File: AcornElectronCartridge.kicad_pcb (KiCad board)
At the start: 2 copper layers, 84.9 x 62.5 mm, 5 parts

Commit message: An intermediate version of a smaller cartridge.
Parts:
- moved Flash1 8.89 mm to (86.4, 104.1)
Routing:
- net /A16: track 82.4 -> 93.0 mm
- net /A10: track 83.4 -> 93.4 mm
- net /A15: track 85.7 -> 95.6 mm
- net /A8: track 56.5 -> 46.8 mm
- net /CSRW: track 84.2 -> 93.6 mm
- net /CE#: track 22.9 -> 31.8 mm
- net /BA7: track 27.2 -> 18.4 mm
- net /BA6: track 27.2 -> 18.4 mm
- net /BA4: track 27.2 -> 18.4 mm
- net /BA3: track 27.2 -> 18.4 mm
- net /BA2: track 27.2 -> 18.4 mm
- net /BA5: track 27.2 -> 18.4 mm
- net /A14: track 5.68 -> 14.2 mm
- net /OE#: track 5.68 -> 14.2 mm
- net /D2: track 26.2 -> 17.8 mm
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
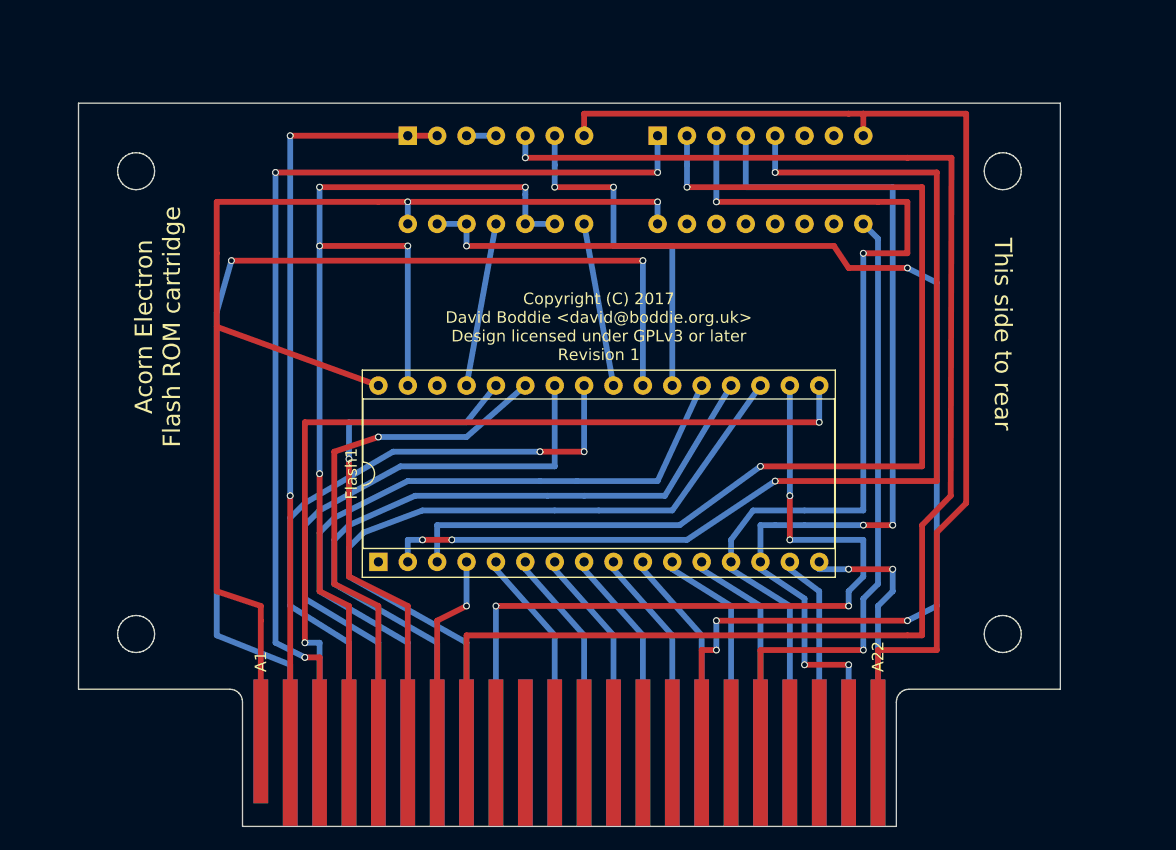
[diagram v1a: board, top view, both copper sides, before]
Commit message: Made space at the top of the board.
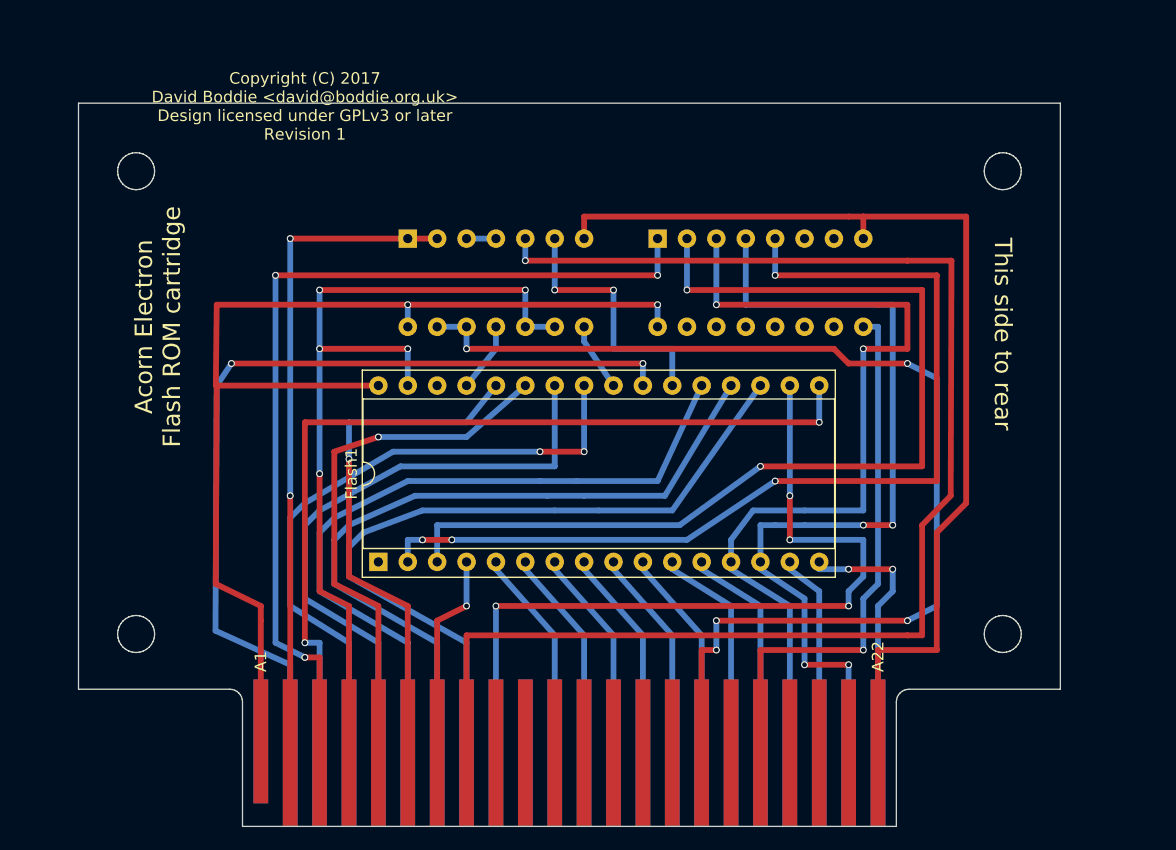
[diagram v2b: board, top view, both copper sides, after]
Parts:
- moved FLIP1 8.89 mm to (110.5, 76.2)
- moved NAND1 8.89 mm to (88.9, 76.2)
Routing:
- net /CSRW: track 93.6 -> 75.9 mm
- net /A10: track 93.4 -> 75.7 mm
- net VCC: track 106.1 -> 96.0 mm
- net GND: track 121.6 -> 112.7 mm
- net /nRST: track 89.2 -> 80.3 mm
- net /nOE: track 66.0 -> 57.2 mm
- net /D1: track 83.3 -> 74.4 mm
- net /CE#: track 31.8 -> 22.9 mm
- net /A15: track 95.6 -> 86.7 mm
- net /D0: track 86.6 -> 77.7 mm
- net /A16: track 93.0 -> 84.1 mm
- net /PHI2: track 130.5 -> 121.7 mm
- net /ROMQA: track 106.4 -> 97.6 mm
- net /OE#: track 14.2 -> 5.85 mm
- net /A14: track 14.2 -> 5.97 mm
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
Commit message: Finished a first draft of the smaller cartridge design.
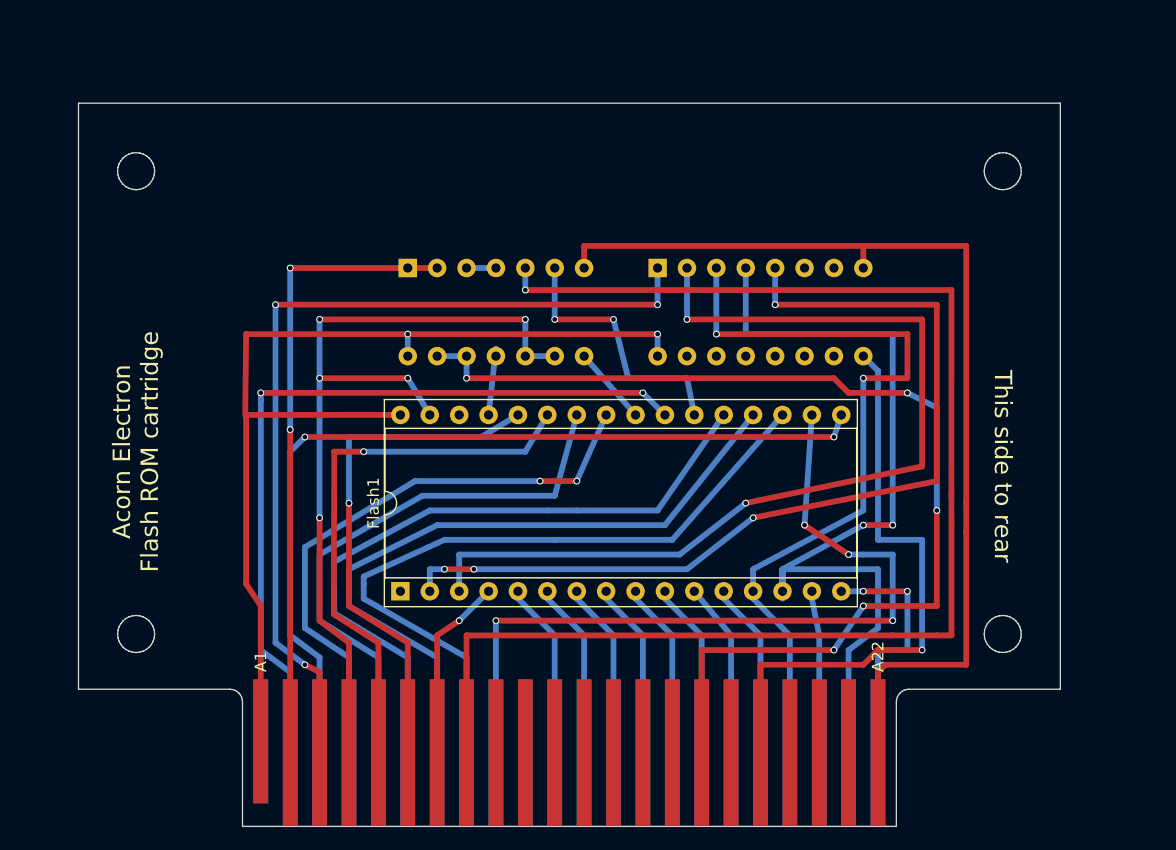
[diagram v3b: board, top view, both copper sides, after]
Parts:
- moved Flash1 3.18 mm to (88.3, 106.7)
- moved FLIP1 2.54 mm to (110.5, 78.7)
- moved NAND1 2.54 mm to (88.9, 78.7)
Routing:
- net /D0: track 77.7 -> 69.3 mm
- net VCC: track 96.0 -> 88.3 mm
- net /A10: track 75.7 -> 68.1 mm
- net /A11: track 56.0 -> 51.2 mm
- net /A9: track 53.4 -> 48.9 mm
- net /nROMSTB: track 47.5 -> 51.9 mm
- net /A15: track 86.7 -> 82.5 mm
- net /A16: track 84.1 -> 79.9 mm
- net /BA0: track 19.3 -> 15.3 mm
- net /D7: track 63.0 -> 59.2 mm
- net /D2: track 17.8 -> 14.0 mm
- net /D6: track 64.3 -> 60.7 mm
- net /D5: track 65.7 -> 62.2 mm
- net /BA1: track 19.3 -> 15.8 mm
- net /ROMQA: track 97.6 -> 94.3 mm
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
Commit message: Placed the smaller chips beside the flash ROM.
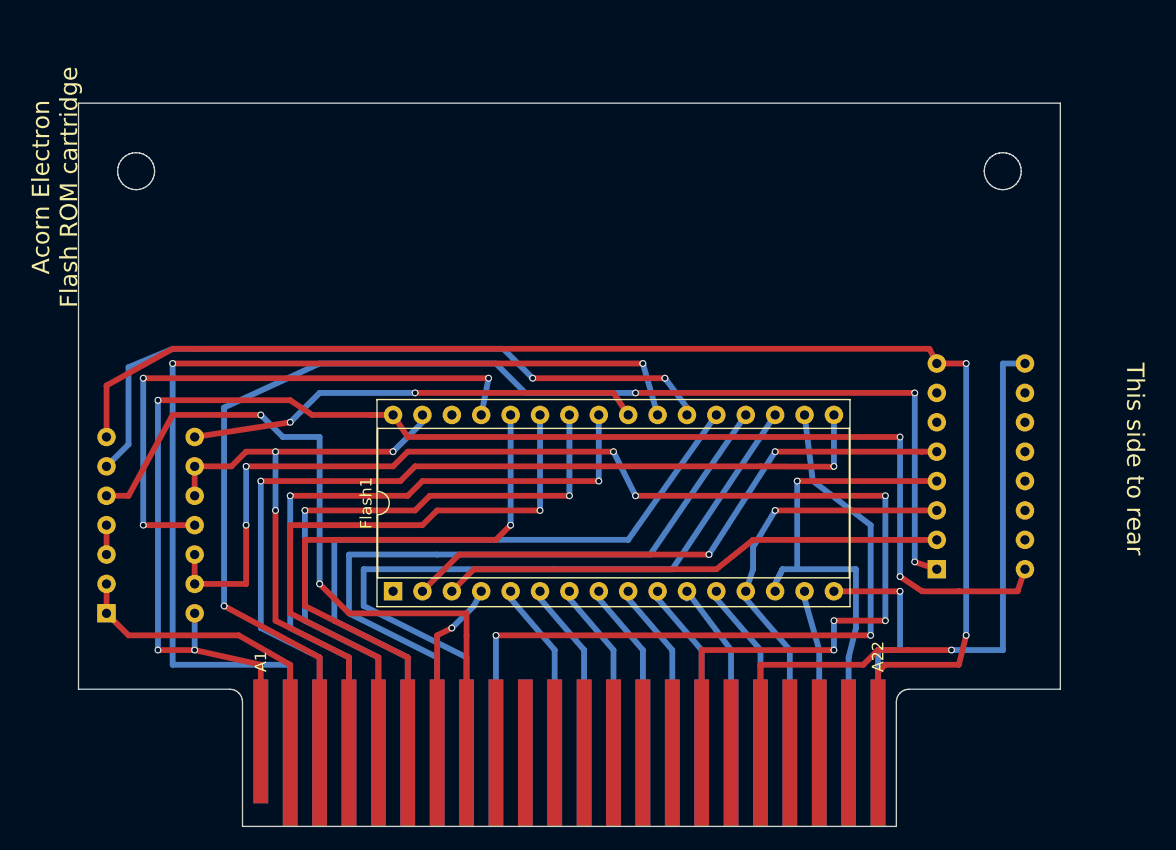
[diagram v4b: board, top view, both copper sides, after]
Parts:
- moved NAND1 39.6 mm to (62.9, 108.6), turned to 0 degrees
- moved FLIP1 35.5 mm to (134.6, 104.8), turned to 0 degrees
- moved Flash1 0.64 mm to (87.6, 106.7)
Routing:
- net /PHI2: track 120.7 -> 61.9 mm, vias 1 -> 2
- net /A14: track 6.39 -> 50.2 mm, vias 0 -> 3
- net VCC: track 88.3 -> 131.2 mm, vias 2 -> 5
- net /A15: track 82.5 -> 43.6 mm, vias 2 -> 0
- net /CE#: track 23.1 -> 61.5 mm, vias 3 -> 2
- net /nRST: track 77.0 -> 113.0 mm, vias 3 -> 4
- net /OE#: track 6.75 -> 39.6 mm, vias 0 -> 2
- net /D0: track 69.3 -> 37.0 mm, vias 2 -> 1
- net GND: track 110.1 -> 142.3 mm, vias 2 -> 3
- net /D1: track 75.9 -> 44.8 mm, vias 2 -> 1
- net /A16: track 79.9 -> 50.6 mm, vias 4 -> 2
- net /nOE: track 54.6 -> 27.5 mm, vias 2 -> 0
- net /A10: track 68.1 -> 89.1 mm
- net /CSRW: track 73.6 -> 54.4 mm, vias 6 -> 3
- net /ROMQA: track 94.3 -> 113.4 mm, vias 5 -> 8
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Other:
- outline, holes or cut-outs redrawn

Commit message: Put all the chips on the same side of the board.
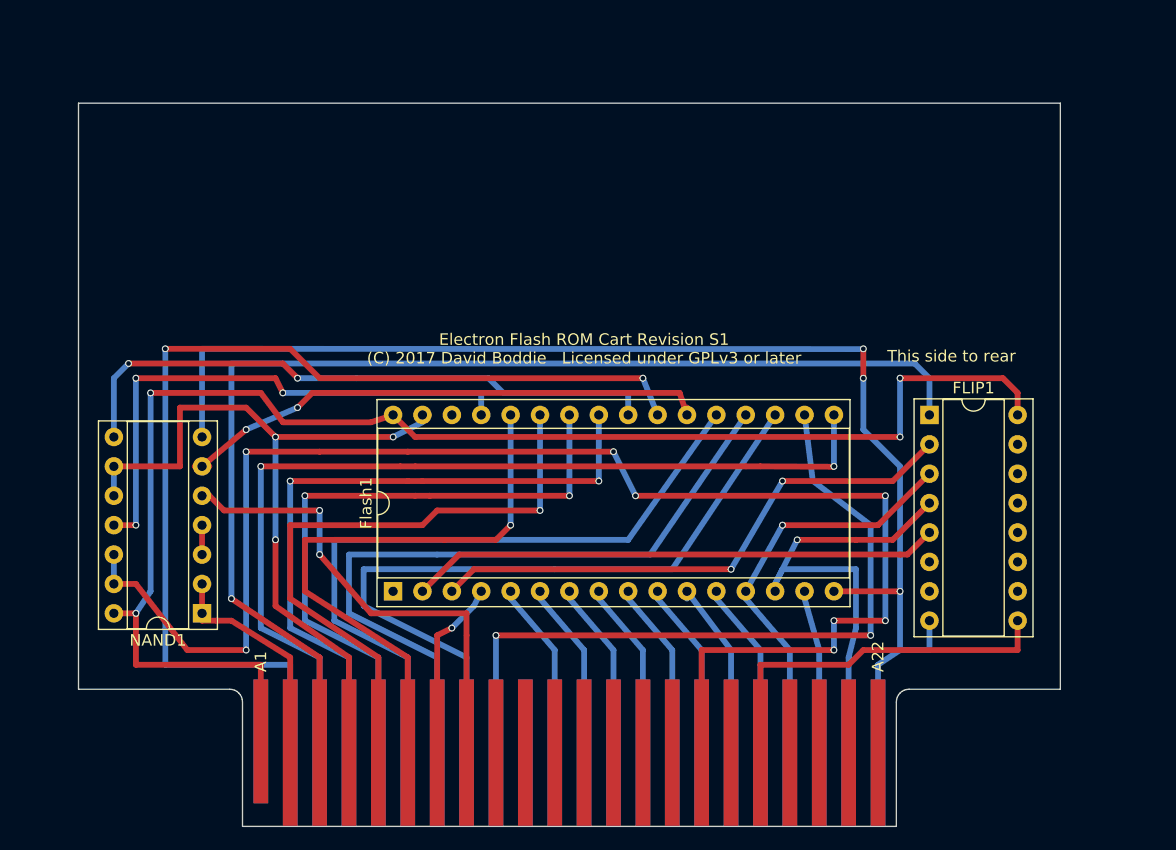
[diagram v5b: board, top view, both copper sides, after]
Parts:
- FLIP1, NAND1: moved to F.Cu
- moved FLIP1 13.4 mm to (134.0, 91.4)
- moved NAND1 8.26 mm to (71.1, 108.6), turned to 180 degrees
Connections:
- CONN1 pad 22: GND -> /0V_A
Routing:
- net GND: track 142.3 -> 112.8 mm
- net /nROMSTB: track 55.8 -> 32.9 mm, vias 1 -> 0
- net /PHI2: track 61.9 -> 42.2 mm
- net /ROMQA: track 113.4 -> 129.6 mm
- net /CE#: track 61.5 -> 47.9 mm
- net /OE#: track 39.6 -> 53.0 mm
- net /CSRW: track 54.4 -> 66.3 mm
- net /nRST: track 113.0 -> 101.8 mm, vias 4 -> 1
- net /nOE: track 27.5 -> 20.0 mm
- net /A16: track 50.6 -> 45.9 mm, vias 2 -> 0
- net /A15: track 43.6 -> 47.8 mm, vias 0 -> 2
- net /D1: track 44.8 -> 40.7 mm
- net VCC: track 131.2 -> 127.8 mm, vias 5 -> 4
- net /A14: track 50.2 -> 47.1 mm
- net /A10: track 89.1 -> 91.5 mm
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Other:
- outline, holes or cut-outs redrawn
- board text added: "Electron Flash ROM Cart Revision S1 (C) 2017 David Boddie Licensed under GPLv3 or later"
- board text removed: "Acorn Electron Flash ROM cartridge"
- board text removed: "Copyright (C) 2017 David Boddie <david@boddie.org.uk> Design licensed under GPLv3 or later Revision 1"

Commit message: Updated the board outline and tidied up tracks and labels.
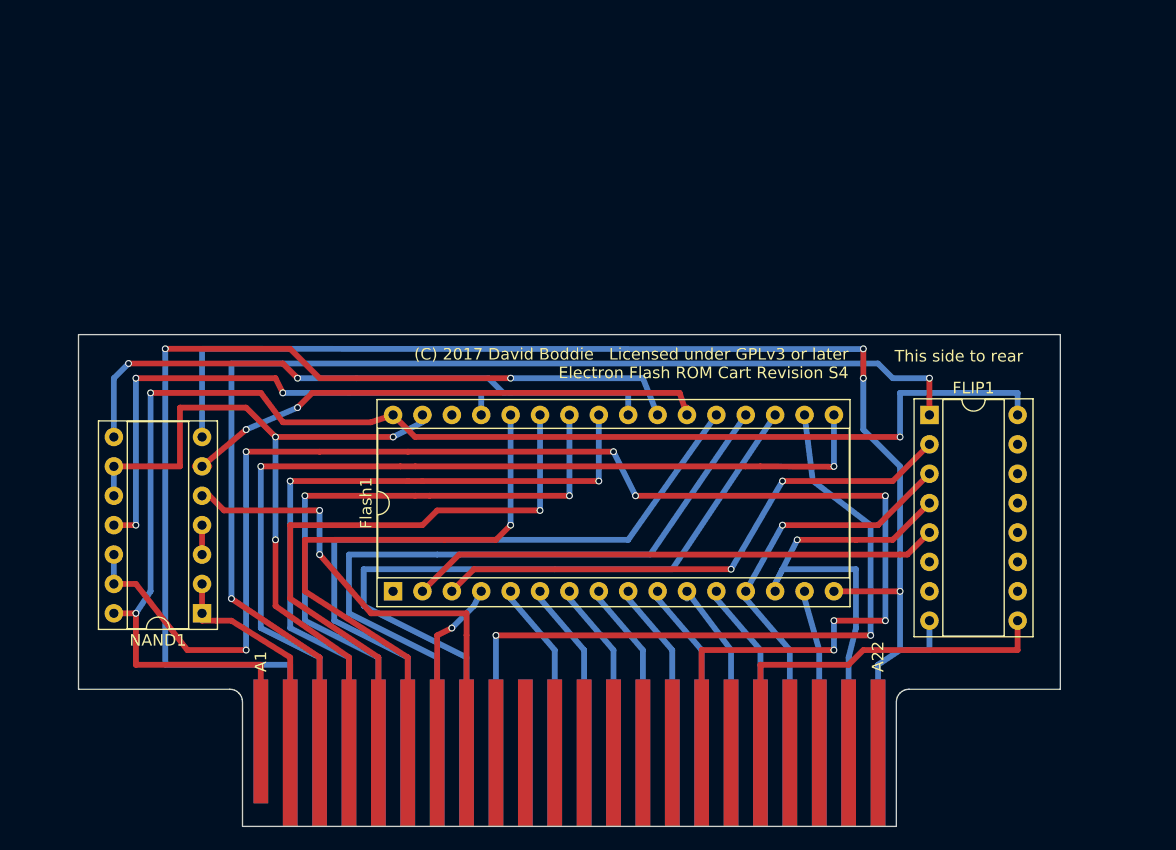
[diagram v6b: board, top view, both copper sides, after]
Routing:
- net VCC: track 127.8 -> 126.0 mm, vias 4 -> 3
- net /nRST: vias 1 -> 2
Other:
- board size 84.9 x 62.5 mm -> 84.9 x 42.5 mm
- board text added: "(C) 2017 David Boddie Licensed under GPLv3 or later Electron Flash ROM Cart Revision S4"
- board text removed: "Electron Flash ROM Cart Revision S1 (C) 2017 David Boddie Licensed under GPLv3 or later"
